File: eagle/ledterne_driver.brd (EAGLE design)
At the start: 24.3 x 23.1 mm, 15 parts, among them IC1 MEGA8-AI

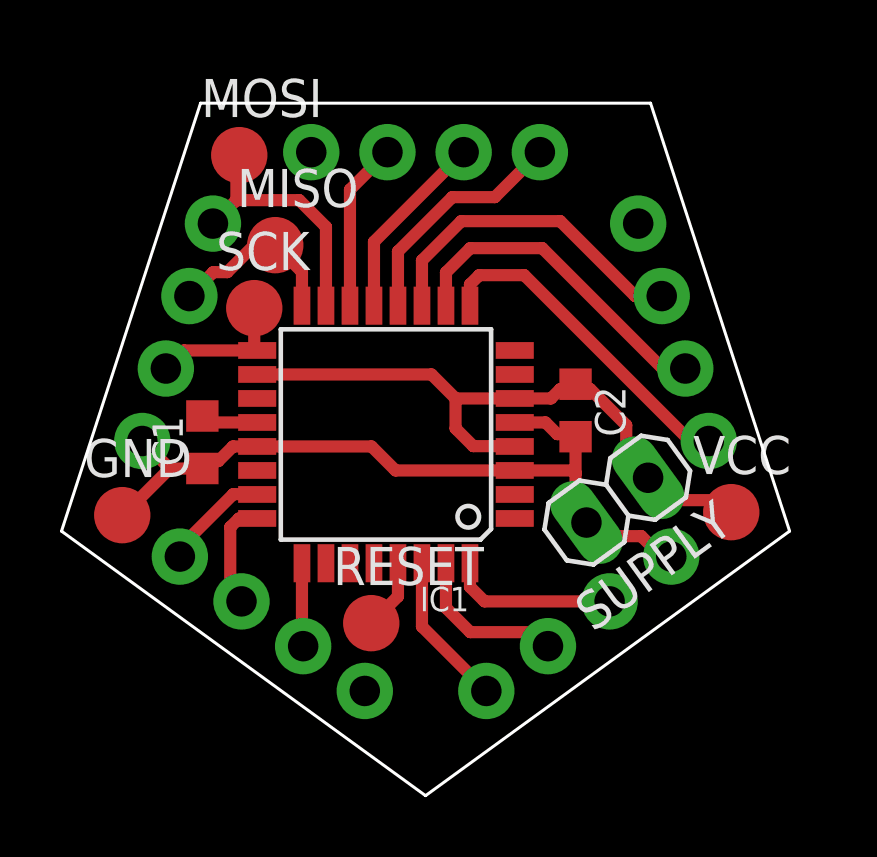
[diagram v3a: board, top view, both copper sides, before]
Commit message: Add ground plane on bottom side
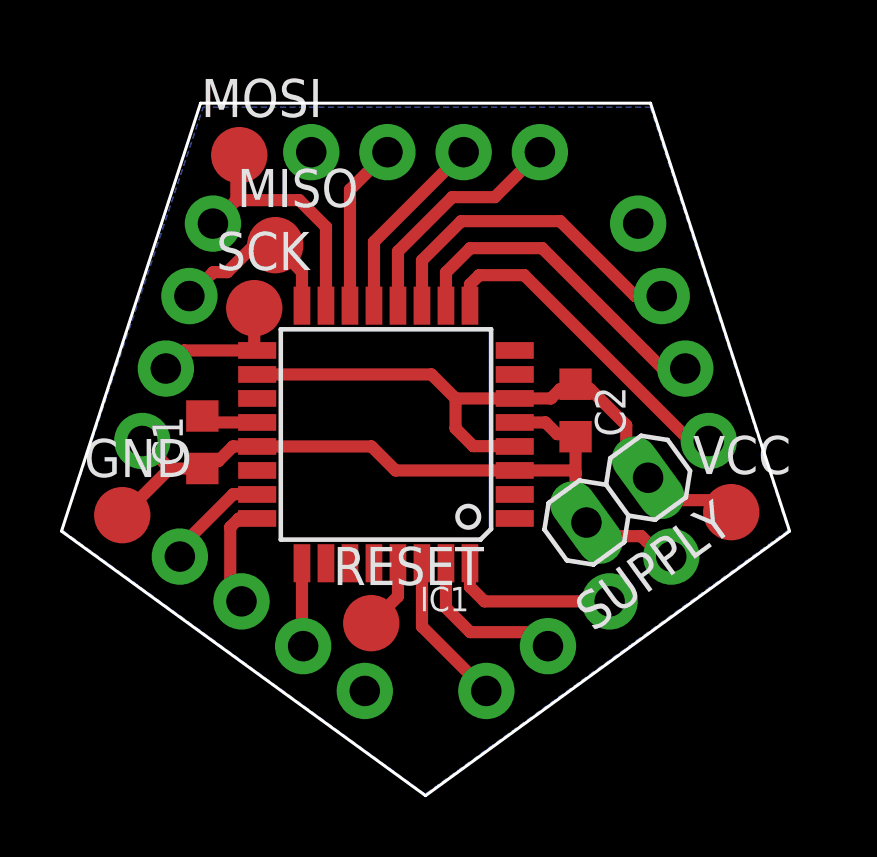
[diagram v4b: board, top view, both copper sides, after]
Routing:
- added copper zone on layer 16, net GND
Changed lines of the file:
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@@
 </class>
 </classes>
-<designrules name="default">
+<designrules name="default *">
 <description language="de">&lt;b&gt;EAGLE Design Rules&lt;/b&gt;
 &lt;p&gt;
@@
 <param name="mdViaViaSameLayer" value="8mil"/>
 <param name="mnLayersViaInSmd" value="2"/>
-<param name="mdCopperDimension" value="40mil"/>
+<param name="mdCopperDimension" value="15mil"/>
 <param name="mdDrill" value="8mil"/>
 <param name="mdSmdStop" value="0mil"/>
@@
 <wire x1="6.4" y1="13.1" x2="6.429796875" y2="13.1" width="0.4064" layer="1"/>
 <wire x1="6.429796875" y1="13.1" x2="7.984796875" y2="14.655" width="0.4064" layer="1"/>
-<wire x1="20.51" y1="16.19" x2="23.597328125" y2="22.81888125" width="0" layer="19" extent="1-1"/>
-<wire x1="14.484503125" y1="7.240178125" x2="15.51" y2="14.59" width="0" layer="19" extent="1-1"/>
-<wire x1="12.7" y1="25.2" x2="10.8974" y2="15.39" width="0" layer="19" extent="1-1"/>
+<polygon width="0.4064" layer="16" isolate="0.5">
+<vertex x="9.1" y="26.7"/>
+<vertex x="24" y="26.7"/>
+<vertex x="28.6" y="12.6"/>
+<vertex x="16.5" y="3.8"/>
+<vertex x="4.4" y="12.6"/>
+</polygon>
 </signal>
 <signal name="VCC">
